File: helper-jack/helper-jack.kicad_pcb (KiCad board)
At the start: 2 copper layers, 12 x 15.5 mm, 4 parts, among them J1 S, J2 TIP, J3 TN, J4 WQP518MA-BM_Combined

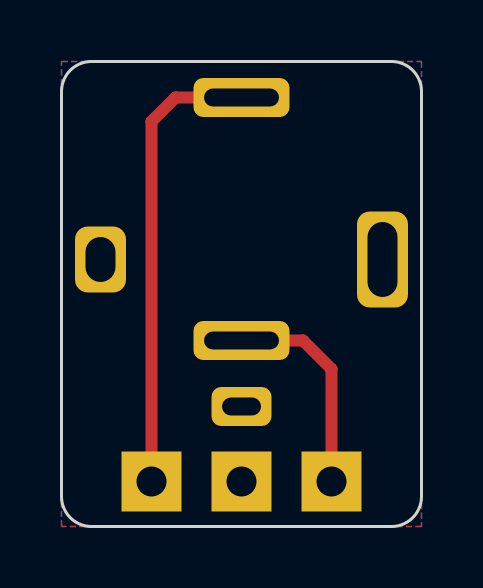
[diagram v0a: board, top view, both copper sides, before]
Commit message: Add markings to switch and jack helpers
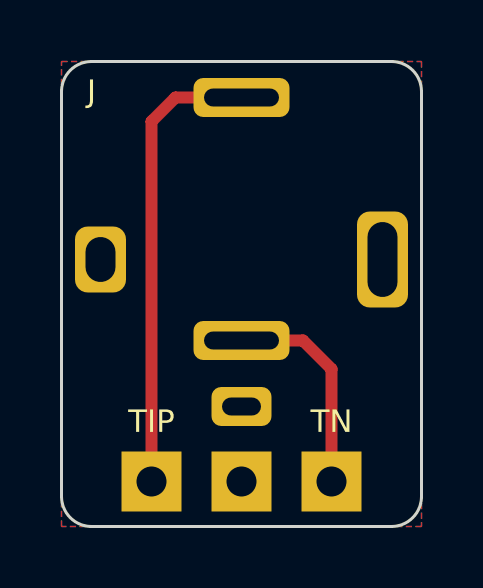
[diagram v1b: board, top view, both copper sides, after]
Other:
- board text added: "J"
- board text added: "TIP"
- board text added: "TN"
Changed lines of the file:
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@@
       (layerselection 0x00010f0_ffffffff)
       (disableapertmacros false)
-      (usegerberextensions false)
-      (usegerberattributes true)
+      (usegerberextensions true)
+      (usegerberattributes false)
       (usegerberadvancedattributes true)
       (creategerberjobfile false)
@@
     )
     (fp_text value "TIP" (at -0.025 2) (layer "B.SilkS")
-      (effects (font (size 0.8 0.8) (thickness 0.15)) (justify mirror))
+      (effects (font (size 0.75 0.75) (thickness 0.15)) (justify mirror))
     )
     (fp_text user "${REFERENCE}" (at 0 2) (layer "B.Fab") hide
@@
     )
     (fp_text value "TN" (at 0 2) (layer "B.SilkS")
-      (effects (font (size 0.8 0.8) (thickness 0.15)) (justify mirror))
+      (effects (font (size 0.75 0.75) (thickness 0.15)) (justify mirror))
     )
     (fp_text user "${REFERENCE}" (at 0 2) (layer "B.Fab") hide
@@
   (gr_line (start 30 35.5) (end 20 35.5) (layer "Edge.Cuts") (width 0.1))
   (gr_arc (start 19 21) (mid 19.292893 20.292893) (end 20 20) (layer "Edge.Cuts") (width 0.1))
+  (gr_text "TIP" (at 22 32) (layer "F.SilkS")
+    (effects (font (size 0.75 0.75) (thickness 0.15)))
+  )
+  (gr_text "J" (at 20 21) (layer "F.SilkS")
+    (effects (font (size 0.75 0.75) (thickness 0.15)))
+  )
+  (gr_text "TN" (at 28 32) (layer "F.SilkS")
+    (effects (font (size 0.75 0.75) (thickness 0.15)))
+  )
   (segment (start 22 34) (end 22 22) (width 0.4) (layer "F.Cu") (net 2))
   (segment (start 22 22) (end 22.8 21.2) (width 0.4) (layer "F.Cu") (net 2))

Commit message: Update helper jack to KiCad 7, Adjust markings, jack footprint
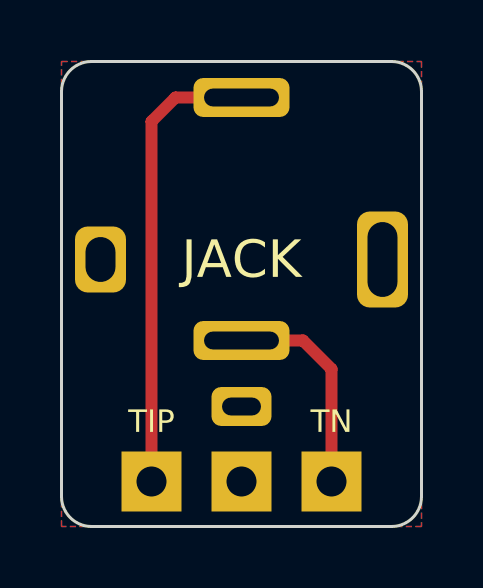
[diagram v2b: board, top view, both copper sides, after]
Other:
- board text added: "JACK"
- board text removed: "J"

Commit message: Fix helper jack copper edge clearance for v-cuts
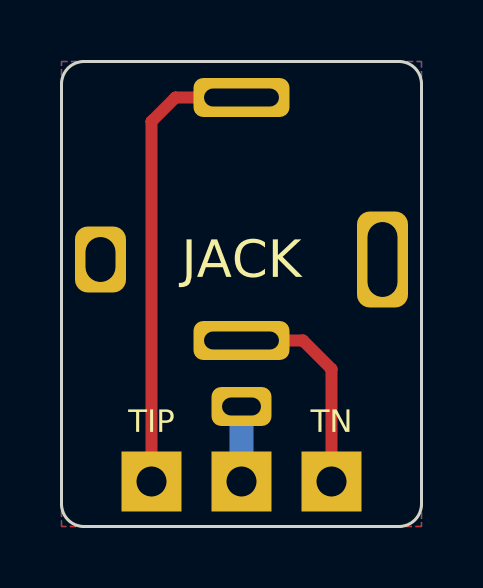
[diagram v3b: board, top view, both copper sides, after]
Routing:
- net /S: track 0.00 -> 2.50 mm
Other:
- outline, holes or cut-outs redrawn
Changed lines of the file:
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@@
     )
   )
-  (gr_line (start 31 21) (end 31 34.5)
+  (gr_line (start 31 20.75) (end 31 34.75)
     (stroke (width 0.1) (type solid)) (layer "Edge.Cuts"))
-  (gr_line (start 19 34.5) (end 19 21)
+  (gr_line (start 19 34.75) (end 19 20.75)
     (stroke (width 0.1) (type solid)) (layer "Edge.Cuts"))
-  (gr_arc (start 31 34.5) (mid 30.707107 35.207107) (end 30 35.5)
+  (gr_arc (start 31 34.75) (mid 30.78033 35.28033) (end 30.25 35.5)
     (stroke (width 0.1) (type solid)) (layer "Edge.Cuts"))
-  (gr_arc (start 20 35.5) (mid 19.292893 35.207107) (end 19 34.5)
+  (gr_arc (start 19.75 35.5) (mid 19.21967 35.28033) (end 19 34.75)
     (stroke (width 0.1) (type solid)) (layer "Edge.Cuts"))
-  (gr_line (start 20 20) (end 30 20)
+  (gr_line (start 19.75 20) (end 30.25 20)
     (stroke (width 0.1) (type solid)) (layer "Edge.Cuts"))
-  (gr_arc (start 30 20) (mid 30.707107 20.292893) (end 31 21)
+  (gr_arc (start 30.25 20) (mid 30.78033 20.21967) (end 31 20.75)
     (stroke (width 0.1) (type solid)) (layer "Edge.Cuts"))
-  (gr_line (start 30 35.5) (end 20 35.5)
+  (gr_line (start 30.25 35.5) (end 19.75 35.5)
     (stroke (width 0.1) (type solid)) (layer "Edge.Cuts"))
-  (gr_arc (start 19 21) (mid 19.292893 20.292893) (end 20 20)
+  (gr_arc (start 19 20.75) (mid 19.21967 20.21967) (end 19.75 20)
     (stroke (width 0.1) (type solid)) (layer "Edge.Cuts"))
   (gr_text "TIP" (at 22 32) (layer "F.SilkS")
@@
     (effects (font (size 0.75 0.75) (thickness 0.15)))
   )
+  (segment (start 25 34) (end 25 31.5) (width 0.8) (layer "B.Cu") (net 1))
   (segment (start 22 34) (end 22 22) (width 0.4) (layer "F.Cu") (net 2))
   (segment (start 22 22) (end 22.8 21.2) (width 0.4) (layer "F.Cu") (net 2))
